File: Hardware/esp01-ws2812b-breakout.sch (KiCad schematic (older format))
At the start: 17 parts, among them J1 Screw_Terminal_01x02, J2 Screw_Terminal_01x04, J3 Conn_01x03_Male, Q1 IRFS4127, Q2 IRFS4127, U1 LM1117-3.3, U2 ESP-01v090, U3 DS18B20

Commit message: Updated capacitor footprint and NETlist
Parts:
- C3: footprint Capacitor_SMD:C_0603_1608Metric_Pad1.08x0.95mm_HandSolder -> Capacitor_THT:CP_Radial_D5.0mm_P2.00mm
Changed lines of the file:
@@
 F 0 "C3" H 5668 2846 50  0000 L CNN
 F 1 "100uF" H 5668 2755 50  0000 L CNN
-F 2 "Capacitor_SMD:C_0603_1608Metric_Pad1.08x0.95mm_HandSolder" H 5588 2650 50  0001 C CNN
+F 2 "Capacitor_THT:CP_Radial_D5.0mm_P2.00mm" H 5588 2650 50  0001 C CNN
 F 3 "~" H 5550 2800 50  0001 C CNN
 	1    5550 2800

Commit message: Finished PCB layout
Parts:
- added H1, H2: MountingHole, MountingHole:MountingHole_2.2mm_M2, symbol Mechanical:MountingHole
- J1: footprint Connector_PinHeader_2.54mm:PinHeader_1x04_P2.54mm_Vertical -> Custom Terminals:0102-blue-terminal
- J2: footprint Connector_PinHeader_2.54mm:PinHeader_1x08_P2.54mm_Vertical -> Custom Terminals:0104-blue-terminal
- Q1, Q2: footprint ESP8266:SOT-23_Handsoldering_DS-REVERSED -> Custom Mosfets:SOT-23_DS-REVERSED
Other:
- note added: "Mounting holes"
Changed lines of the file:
@@
 F 0 "J1" H 1068 1025 50  0000 C CNN
 F 1 "Screw_Terminal_01x02" H 1068 1116 50  0000 C CNN
-F 2 "Connector_PinHeader_2.54mm:PinHeader_1x04_P2.54mm_Vertical" H 1150 1350 50  0001 C CNN
+F 2 "Custom Terminals:0102-blue-terminal" H 1150 1350 50  0001 C CNN
 F 3 "~" H 1150 1350 50  0001 C CNN
 	1    1150 1350
@@
 F 0 "J2" H 6380 2992 50  0000 L CNN
 F 1 "Screw_Terminal_01x04" H 6380 2901 50  0000 L CNN
-F 2 "Connector_PinHeader_2.54mm:PinHeader_1x08_P2.54mm_Vertical" H 6300 3000 50  0001 C CNN
+F 2 "Custom Terminals:0104-blue-terminal" H 6300 3000 50  0001 C CNN
 F 3 "~" H 6300 3000 50  0001 C CNN
 	1    6300 3000
@@
 F 0 "Q1" V 1949 3050 50  0000 C CNN
 F 1 "IRFS4127" V 2040 3050 50  0000 C CNN
-F 2 "ESP8266:SOT-23_Handsoldering_DS-REVERSED" H 1900 2975 50  0001 L CIN
+F 2 "Custom Mosfets:SOT-23_DS-REVERSED" H 1900 2975 50  0001 L CIN
 F 3 "https://www.infineon.com/dgdl/irfs4127pbf.pdf?fileId=5546d462533600a401535636ee7b2192" H 1700 3050 50  0001 L CNN
 	1    1700 3050
@@
 F 0 "Q2" V 4199 3050 50  0000 C CNN
 F 1 "IRFS4127" V 4290 3050 50  0000 C CNN
-F 2 "ESP8266:SOT-23_Handsoldering_DS-REVERSED" H 4150 2975 50  0001 L CIN
+F 2 "Custom Mosfets:SOT-23_DS-REVERSED" H 4150 2975 50  0001 L CIN
 F 3 "https://www.infineon.com/dgdl/irfs4127pbf.pdf?fileId=5546d462533600a401535636ee7b2192" H 3950 3050 50  0001 L CNN
 	1    3950 3050
@@
 Wire Wire Line
 	7950 3000 7850 3000
+$Comp
+L Mechanical:MountingHole H1
+U 1 1 5FE31388
+P 750 4350
+F 0 "H1" H 850 4396 50  0000 L CNN
+F 1 "MountingHole" H 850 4305 50  0000 L CNN
+F 2 "MountingHole:MountingHole_2.2mm_M2" H 750 4350 50  0001 C CNN
+F 3 "~" H 750 4350 50  0001 C CNN
+	1    750  4350
+	1    0    0    -1
+$EndComp
+$Comp
+L Mechanical:MountingHole H2
+U 1 1 5FE31DB5
+P 750 4650
+F 0 "H2" H 850 4696 50  0000 L CNN
+F 1 "MountingHole" H 850 4605 50  0000 L CNN
+F 2 "MountingHole:MountingHole_2.2mm_M2" H 750 4650 50  0001 C CNN
+F 3 "~" H 750 4650 50  0001 C CNN
+	1    750  4650
+	1    0    0    -1
+$EndComp
+Wire Notes Line
+	2750 3750 2750 5350
+Wire Notes Line
+	500  5350 2750 5350
+Text Notes 550  5300 0    50   ~ 0
+Mounting holes
 $EndSCHEMATC

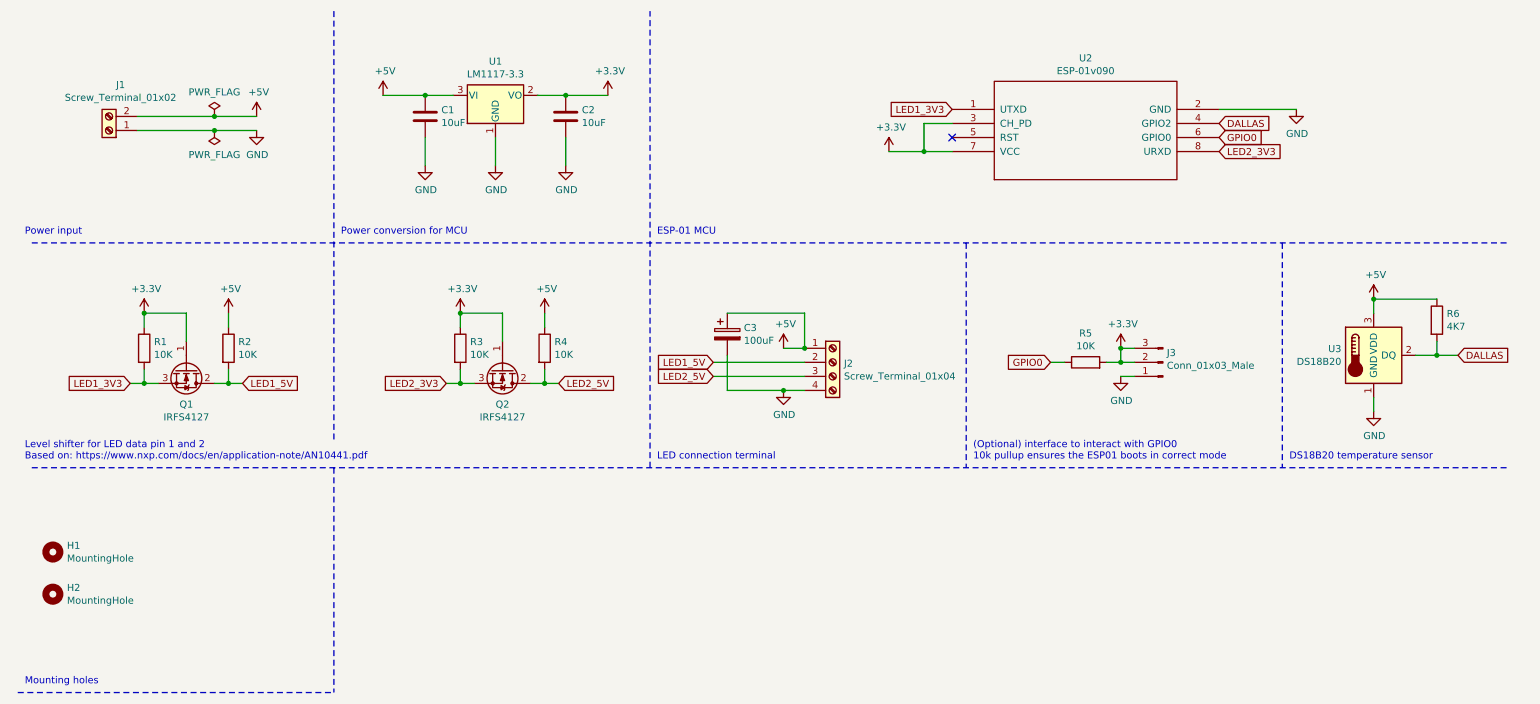
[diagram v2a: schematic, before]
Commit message: Changed decoupling capacitors layout
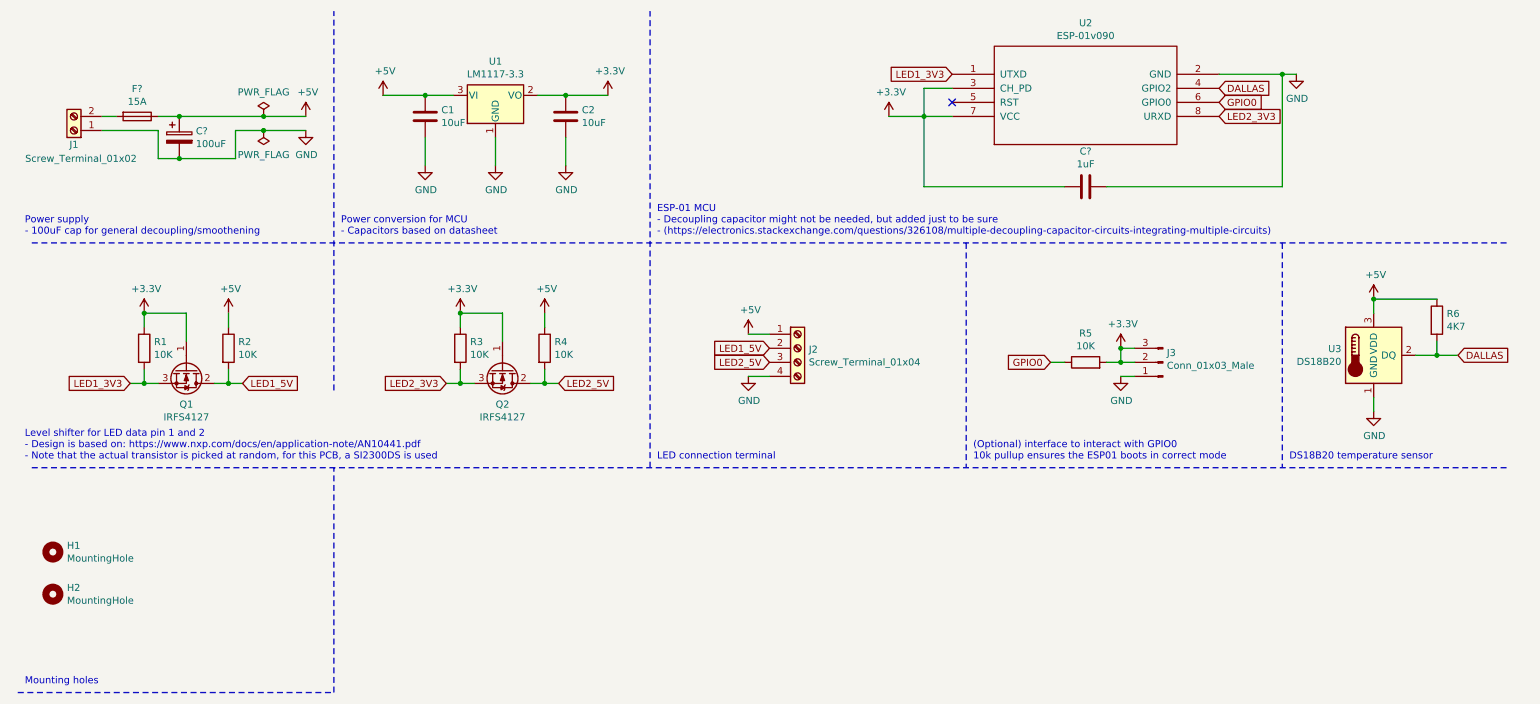
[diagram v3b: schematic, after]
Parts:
- removed C3: 100uF, Capacitor_THT:CP_Radial_D5.0mm_P2.00mm, symbol Device:CP
- added C?: 1uF, symbol Device:C
- added C?: 100uF, symbol Device:CP
- added F?: 15A, symbol Device:Fuse
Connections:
- net +3V3: now also C?.2
- net +5V: now also C?.1, F?.1; no longer J1.2 (Pin_2)
- net GND: now also C?.1, C?.2
- new net: F?.2, J1.2 (Pin_2)
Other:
- note added: "ESP-01 MCU\n- Decoupling capacitor might not be needed, but added just to be sure \n- (https://electronics.stackexchange.com/questions/326108/multiple-decoupling-capacitor-circuits-integrating-multiple-circuits)"
- note added: "Level shifter for LED data pin 1 and 2 \n- Design is based on: https://www.nxp.com/docs/en/application-note/AN10441.pdf\n- Note that the actual transistor is picked at random, for this PCB, a SI2300DS is used"
- note added: "Power conversion for MCU\n- Capacitors based on datasheet"
- note added: "Power supply\n- 100uF cap for general decoupling/smoothening"
- note removed: "ESP-01 MCU"
- note removed: "Level shifter for LED data pin 1 and 2 \nBased on: https://www.nxp.com/docs/en/application-note/AN10441.pdf"
- note removed: "Power conversion for MCU"
- note removed: "Power input"
- moved on the sheet: J1, J2, U2

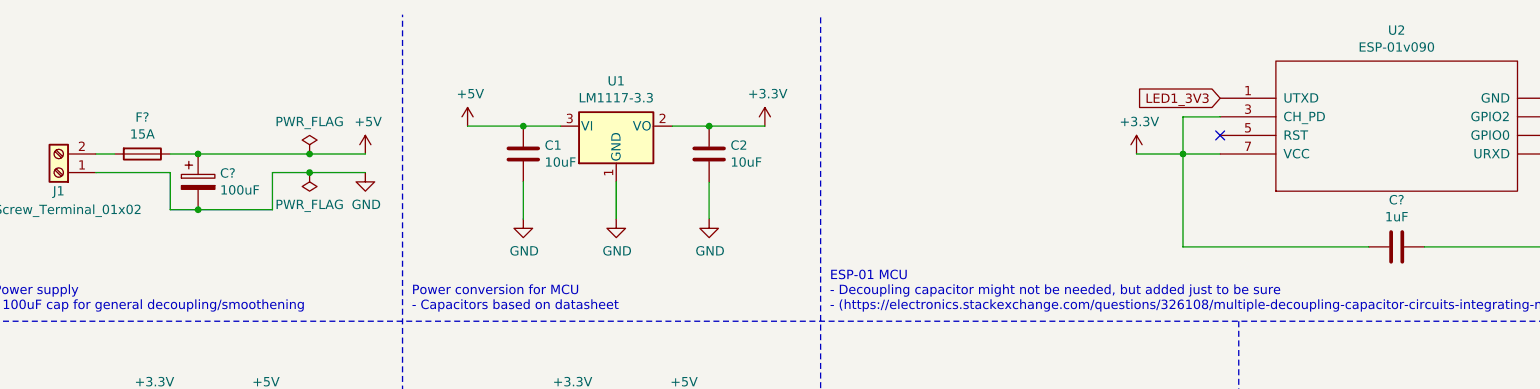
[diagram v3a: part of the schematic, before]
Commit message: Defined footprints and added SMD fuse print
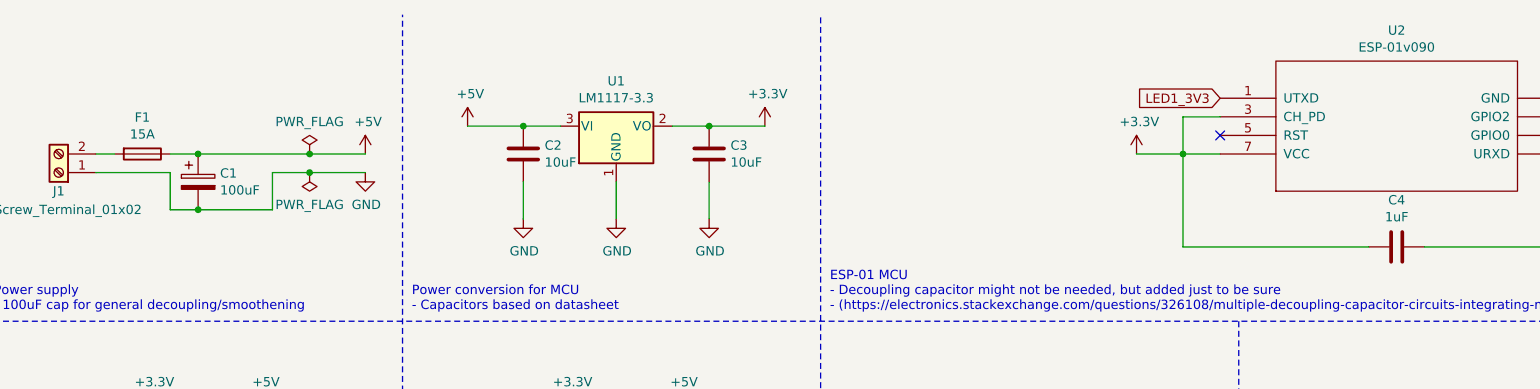
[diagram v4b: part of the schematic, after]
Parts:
- C1: renamed from C?; footprint (none) -> Capacitor_THT:CP_Radial_D5.0mm_P2.00mm
- C2: renamed from C1; footprint Capacitor_SMD:C_0603_1608Metric_Pad1.08x0.95mm_HandSolder -> Capacitor_SMD:C_0805_2012Metric_Pad1.18x1.45mm_HandSolder
- C3: renamed from C2; footprint Capacitor_SMD:C_0603_1608Metric_Pad1.08x0.95mm_HandSolder -> Capacitor_SMD:C_0805_2012Metric_Pad1.18x1.45mm_HandSolder
- C4: renamed from C?; footprint (none) -> Capacitor_SMD:C_0805_2012Metric_Pad1.18x1.45mm_HandSolder
- gave numbers to parts that had none: 1
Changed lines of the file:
@@
 	3400 1100 3600 1100
 $Comp
-L Device:C C2
+L Device:C C3
 U 1 1 5FDF7377
 P 4400 1250
-F 0 "C2" H 4515 1296 50  0000 L CNN
+F 0 "C3" H 4515 1296 50  0000 L CNN
 F 1 "10uF" H 4515 1205 50  0000 L CNN
-F 2 "Capacitor_SMD:C_0603_1608Metric_Pad1.08x0.95mm_HandSolder" H 4438 1100 50  0001 C CNN
+F 2 "Capacitor_SMD:C_0805_2012Metric_Pad1.18x1.45mm_HandSolder" H 4438 1100 50  0001 C CNN
 F 3 "~" H 4400 1250 50  0001 C CNN
 	1    4400 1250
@@
 $EndComp
 $Comp
-L Device:C C1
+L Device:C C2
 U 1 1 5FDF6DA0
 P 3400 1250
-F 0 "C1" H 3515 1296 50  0000 L CNN
+F 0 "C2" H 3515 1296 50  0000 L CNN
 F 1 "10uF" H 3515 1205 50  0000 L CNN
-F 2 "Capacitor_SMD:C_0603_1608Metric_Pad1.08x0.95mm_HandSolder" H 3438 1100 50  0001 C CNN
+F 2 "Capacitor_SMD:C_0805_2012Metric_Pad1.18x1.45mm_HandSolder" H 3438 1100 50  0001 C CNN
 F 3 "~" H 3400 1250 50  0001 C CNN
 	1    3400 1250
@@
 Mounting holes
 $Comp
-L Device:Fuse F?
+L Device:Fuse F1
 U 1 1 5FE51D8D
 P 1350 1250
-F 0 "F?" V 1153 1250 50  0000 C CNN
+F 0 "F1" V 1153 1250 50  0000 C CNN
 F 1 "15A" V 1244 1250 50  0000 C CNN
 F 2 "" V 1280 1250 50  0001 C CNN
@@
 	2750 3200 2750 500
 $Comp
-L Device:C C?
+L Device:C C4
 U 1 1 5FE5DACE
 P 8100 1750
-F 0 "C?" V 7848 1750 50  0000 C CNN
+F 0 "C4" V 7848 1750 50  0000 C CNN
 F 1 "1uF" V 7939 1750 50  0000 C CNN
-F 2 "" H 8138 1600 50  0001 C CNN
+F 2 "Capacitor_SMD:C_0805_2012Metric_Pad1.18x1.45mm_HandSolder" H 8138 1600 50  0001 C CNN
 F 3 "~" H 8100 1750 50  0001 C CNN
 	1    8100 1750
@@
 	9500 950  9600 950
 $Comp
-L Device:CP C?
+L Device:CP C1
 U 1 1 5FE71E53
 P 1650 1400
-F 0 "C?" H 1768 1446 50  0000 L CNN
+F 0 "C1" H 1768 1446 50  0000 L CNN
 F 1 "100uF" H 1768 1355 50  0000 L CNN
-F 2 "" H 1688 1250 50  0001 C CNN
+F 2 "Capacitor_THT:CP_Radial_D5.0mm_P2.00mm" H 1688 1250 50  0001 C CNN
 F 3 "~" H 1650 1400 50  0001 C CNN
 	1    1650 1400

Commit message: Finished schematics and footprint revisions
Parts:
- F1: footprint (none) -> Custom Fuses:1808_SMD_Fuse_Holder
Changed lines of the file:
@@
 F 0 "F1" V 1153 1250 50  0000 C CNN
 F 1 "15A" V 1244 1250 50  0000 C CNN
-F 2 "" V 1280 1250 50  0001 C CNN
+F 2 "Custom Fuses:1808_SMD_Fuse_Holder" V 1280 1250 50  0001 C CNN
 F 3 "~" H 1350 1250 50  0001 C CNN
 	1    1350 1250

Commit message: Resistor footprints were still 0603, fixed now.
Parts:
- R1, R2, R3, R4, R5, R6: footprint Resistor_SMD:R_0603_1608Metric_Pad0.98x0.95mm_HandSolder -> Resistor_SMD:R_0805_2012Metric_Pad1.20x1.40mm_HandSolder
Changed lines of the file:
@@
 F 0 "R6" H 10670 2746 50  0000 L CNN
 F 1 "4K7" H 10670 2655 50  0000 L CNN
-F 2 "Resistor_SMD:R_0603_1608Metric_Pad0.98x0.95mm_HandSolder" V 10530 2700 50  0001 C CNN
+F 2 "Resistor_SMD:R_0805_2012Metric_Pad1.20x1.40mm_HandSolder" V 10530 2700 50  0001 C CNN
 F 3 "~" H 10600 2700 50  0001 C CNN
 	1    10600 2700
@@
 F 0 "R1" H 1470 2946 50  0000 L CNN
 F 1 "10K" H 1470 2855 50  0000 L CNN
-F 2 "Resistor_SMD:R_0603_1608Metric_Pad0.98x0.95mm_HandSolder" V 1330 2900 50  0001 C CNN
+F 2 "Resistor_SMD:R_0805_2012Metric_Pad1.20x1.40mm_HandSolder" V 1330 2900 50  0001 C CNN
 F 3 "~" H 1400 2900 50  0001 C CNN
 	1    1400 2900
@@
 F 0 "R2" H 2070 2946 50  0000 L CNN
 F 1 "10K" H 2070 2855 50  0000 L CNN
-F 2 "Resistor_SMD:R_0603_1608Metric_Pad0.98x0.95mm_HandSolder" V 1930 2900 50  0001 C CNN
+F 2 "Resistor_SMD:R_0805_2012Metric_Pad1.20x1.40mm_HandSolder" V 1930 2900 50  0001 C CNN
 F 3 "~" H 2000 2900 50  0001 C CNN
 	1    2000 2900
@@
 F 0 "R3" H 3720 2946 50  0000 L CNN
 F 1 "10K" H 3720 2855 50  0000 L CNN
-F 2 "Resistor_SMD:R_0603_1608Metric_Pad0.98x0.95mm_HandSolder" V 3580 2900 50  0001 C CNN
+F 2 "Resistor_SMD:R_0805_2012Metric_Pad1.20x1.40mm_HandSolder" V 3580 2900 50  0001 C CNN
 F 3 "~" H 3650 2900 50  0001 C CNN
 	1    3650 2900
@@
 F 0 "R4" H 4320 2946 50  0000 L CNN
 F 1 "10K" H 4320 2855 50  0000 L CNN
-F 2 "Resistor_SMD:R_0603_1608Metric_Pad0.98x0.95mm_HandSolder" V 4180 2900 50  0001 C CNN
+F 2 "Resistor_SMD:R_0805_2012Metric_Pad1.20x1.40mm_HandSolder" V 4180 2900 50  0001 C CNN
 F 3 "~" H 4250 2900 50  0001 C CNN
 	1    4250 2900
@@
 F 0 "R5" V 8307 3000 50  0000 C CNN
 F 1 "10K" V 8216 3000 50  0000 C CNN
-F 2 "Resistor_SMD:R_0603_1608Metric_Pad0.98x0.95mm_HandSolder" V 8030 3000 50  0001 C CNN
+F 2 "Resistor_SMD:R_0805_2012Metric_Pad1.20x1.40mm_HandSolder" V 8030 3000 50  0001 C CNN
 F 3 "~" H 8100 3000 50  0001 C CNN
 	1    8100 3000
